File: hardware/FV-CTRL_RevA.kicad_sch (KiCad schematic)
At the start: 69 parts, among them J1 12V_IN, J10 IR_RX2, J11 IR_TX1 (Col 1), J12 IR_TX2 (Col 2), J13 LS1 (DNP), J14 LS2 (DNP), J15 LS3 (DNP), J16 LS4 (DNP), J17 I2C_RESERVED, J2 XL4015_A (6.0V >=5A), J3 XL4015_B (6.0V >=5A), J4 BUCK_5V (Logic), J5 S1_TOP, J6 S1_BOT, J7 S2_TOP, J8 S2_BOT, J9 IR_RX1, Q1 IRF9540N, Q2 S8050

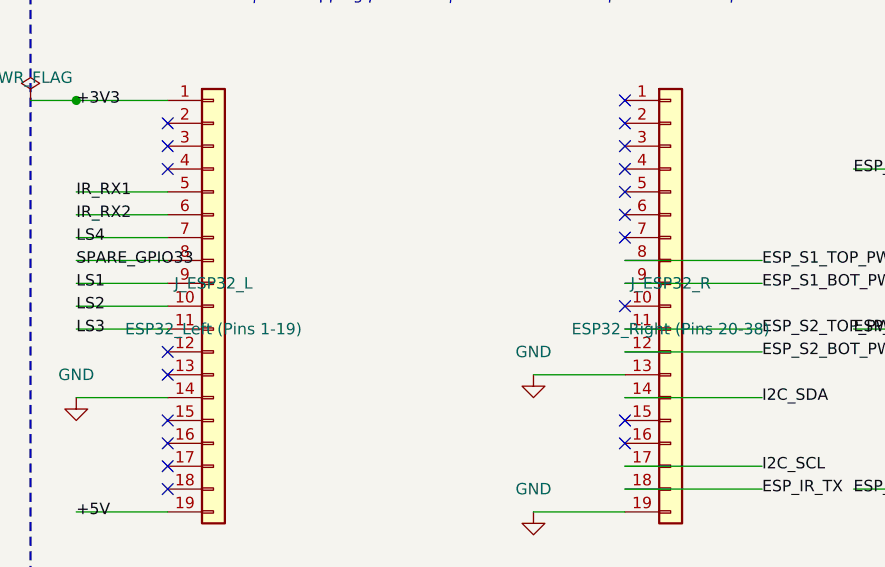
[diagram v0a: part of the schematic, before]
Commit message: fix(sch): standardize ESP32 header references to J18/J19 and update audit status
- Rename J_ESP32_L / J_ESP32_R to standard KiCad annotations J18 / J19
- Regenerate KiCad schematic, manifest, netlist JSON, draft BOM, and ERC reports
- Eliminate netlist export annotation warnings
- Update automated tests in test_code_generation.py for J18 and J19
- Resolve contradiction in audit_fv_project.py and audit-revA.md regarding schematic existence
- Track AGENTS.md rules
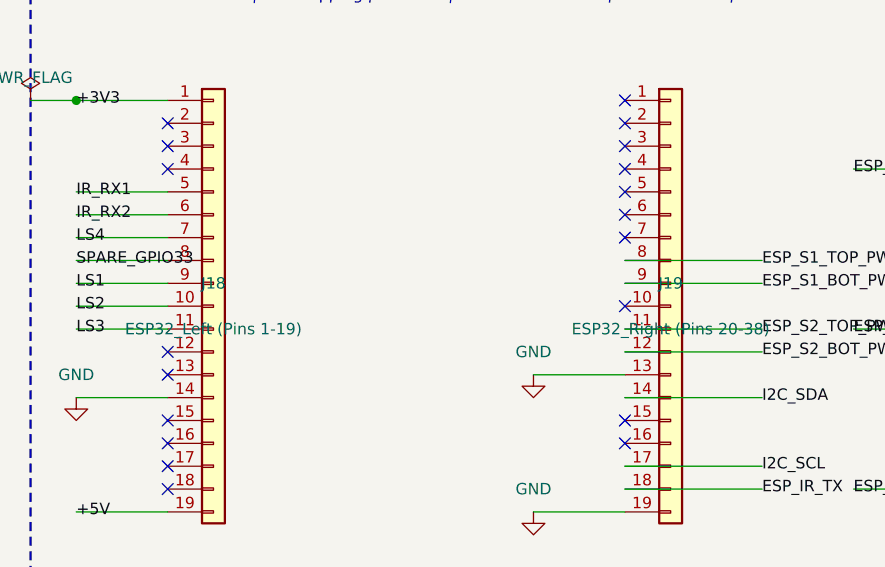
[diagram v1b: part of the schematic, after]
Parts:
- removed J_ESP32_L: ESP32_Left (Pins 1-19), symbol Connector_Generic:Conn_01x19
- removed J_ESP32_R: ESP32_Right (Pins 20-38), symbol Connector_Generic:Conn_01x19
- added J18: ESP32_Left (Pins 1-19), symbol Connector_Generic:Conn_01x19
- added J19: ESP32_Right (Pins 20-38), symbol Connector_Generic:Conn_01x19
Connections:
- net +3V3: now also J18.1 (Pin_1)
- net +5V: now also J18.19 (Pin_19)
- net ESP_IR_TX: now also J19.18 (Pin_18)
- net ESP_S1_BOT_PWM: now also J19.9 (Pin_9)
- net ESP_S1_TOP_PWM: now also J19.8 (Pin_8)
- net ESP_S2_BOT_PWM: now also J19.12 (Pin_12)
- net ESP_S2_TOP_PWM: now also J19.11 (Pin_11)
- net GND: now also J18.14 (Pin_14), J19.13 (Pin_13), J19.19 (Pin_19)
- net I2C_SCL: now also J19.17 (Pin_17)
- net I2C_SDA: now also J19.14 (Pin_14)
- net IR_RX1: now also J18.5 (Pin_5)
- net IR_RX2: now also J18.6 (Pin_6)
- net LS1: now also J18.9 (Pin_9)
- net LS2: now also J18.10 (Pin_10)
- net LS3: now also J18.11 (Pin_11)
- net LS4: now also J18.7 (Pin_7)
- net SPARE_GPIO33: now also J18.8 (Pin_8)
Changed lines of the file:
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@@
 		(on_board yes)
 		(dnp no)
-		(property "Reference" "J_ESP32_L"
+		(property "Reference" "J18"
 			(at 152.4000 154.9400 0)
 			(effects (font (size 1.27 1.27)))
@@
 		(on_board yes)
 		(dnp no)
-		(property "Reference" "J_ESP32_R"
+		(property "Reference" "J19"
 			(at 203.2000 154.9400 0)
 			(effects (font (size 1.27 1.27)))

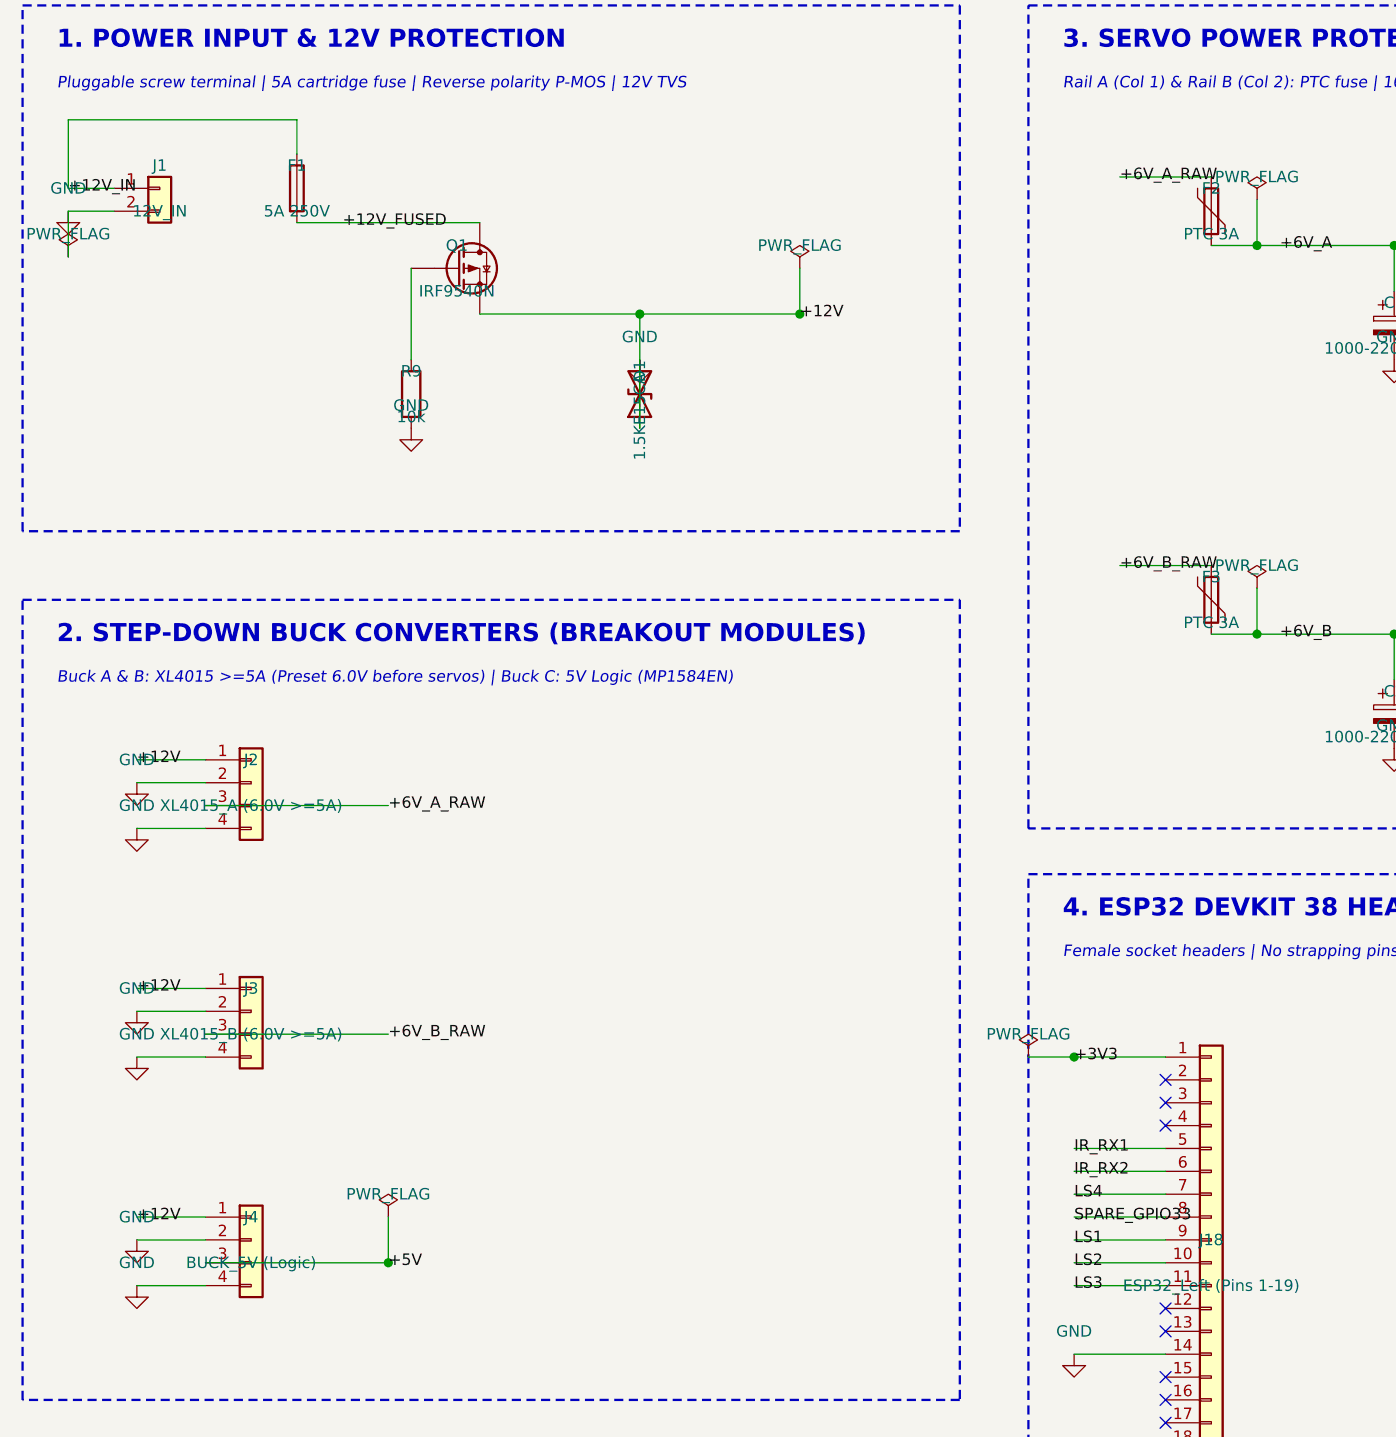
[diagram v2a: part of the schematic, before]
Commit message: feat(sch): synchronize schematics, manifests, and zero-violation ERC reports
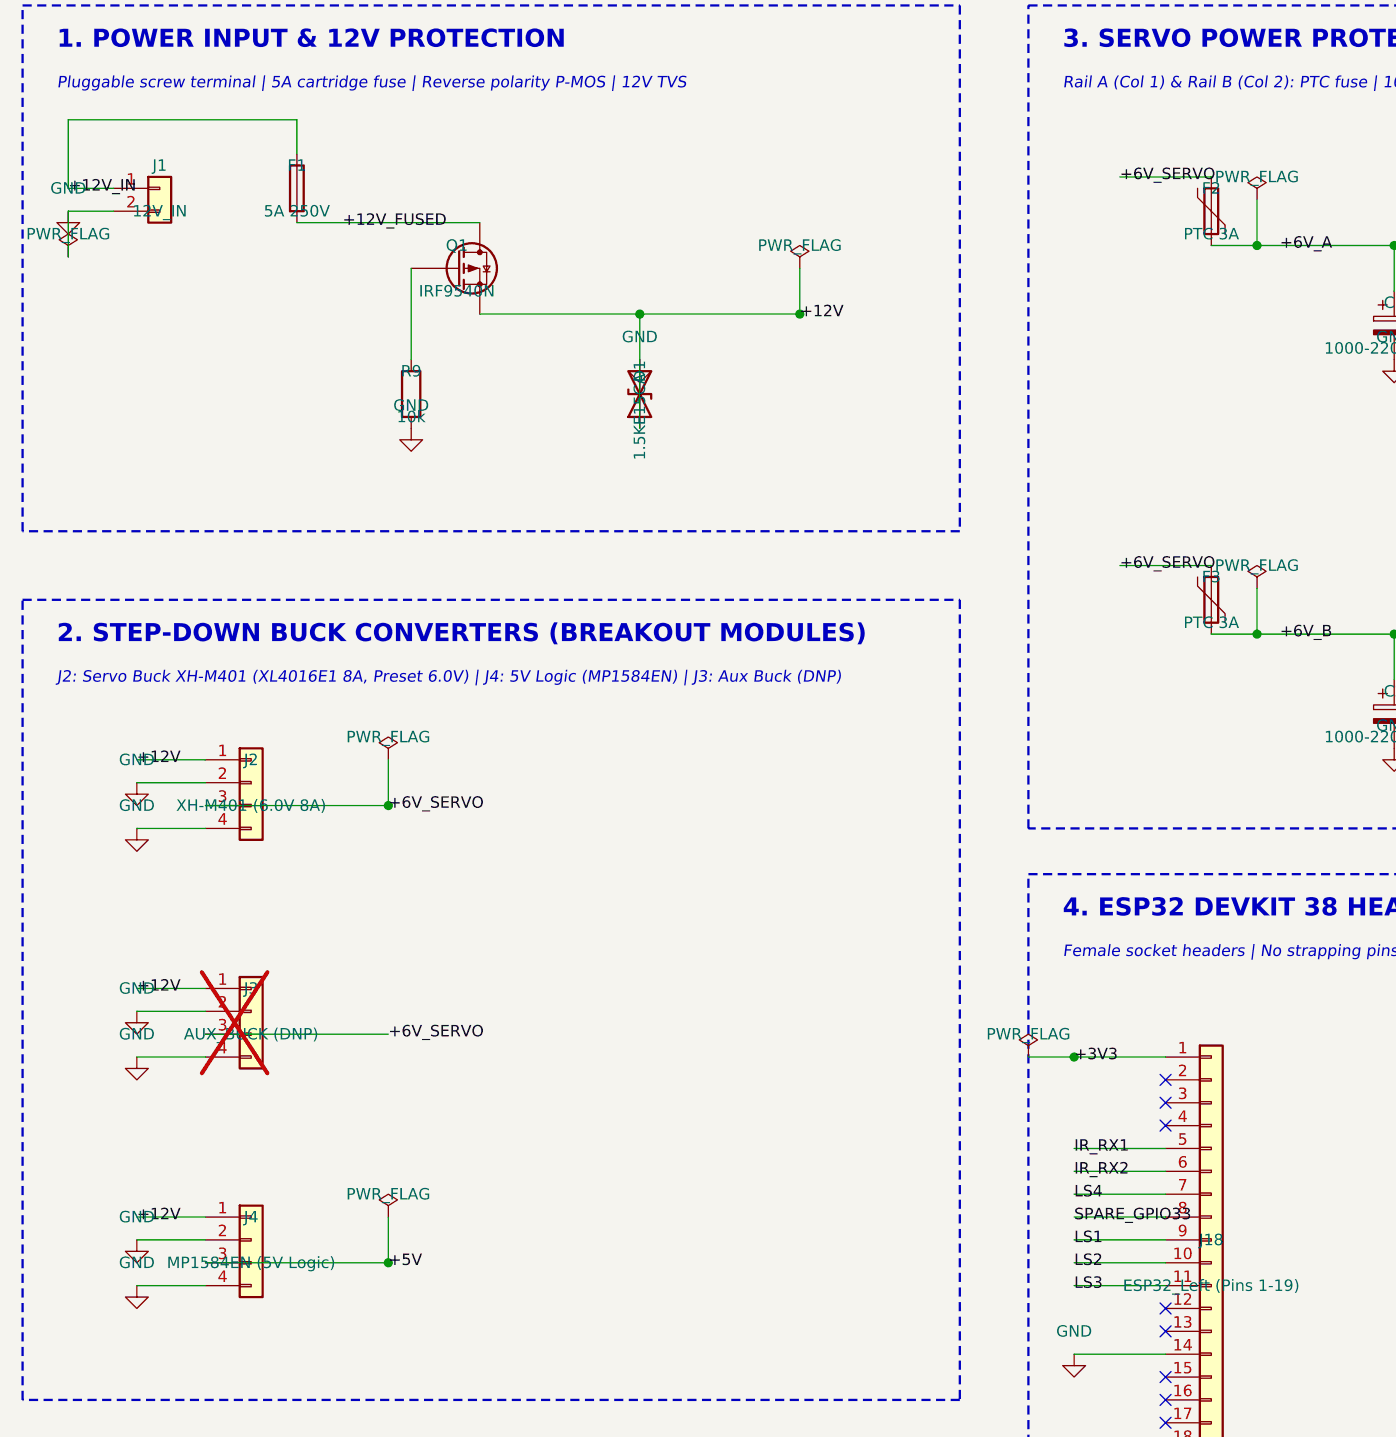
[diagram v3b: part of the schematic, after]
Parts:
- C1, C2: footprint (none) -> Capacitor_THT:CP_Radial_D12.5mm_P5.00mm
- C10, C3, C4, C5, C6, C7, C8, C9: footprint (none) -> Capacitor_THT:C_Disc_D5.0mm_W2.5mm_P5.00mm
- D1: footprint (none) -> Diode_THT:D_DO-201_P12.70mm_Horizontal
- D2, D3, D4, D5, D6: footprint (none) -> LED_THT:LED_D3.0mm
- F1: footprint (none) -> Fuse:Fuseholder_Clip-5x20mm_Littelfuse_111_Inline_P20.00x5.00mm_D1.05mm_Horizontal
- F2, F3: footprint (none) -> Fuse:Fuse_Bourns_MF-RG300
- J1: footprint (none) -> TerminalBlock_Phoenix:TerminalBlock_Phoenix_MKDS-1,5-2-5.08_1x02_P5.08mm_Horizontal
- J10, J9: footprint (none) -> Connector_JST:JST_XH_B3B-XH-A_1x03_P2.50mm_Vertical
- J11, J12, J13, J14, J15, J16: footprint (none) -> Connector_JST:JST_XH_B2B-XH-A_1x02_P2.50mm_Vertical
- J17: footprint (none) -> Connector_PinHeader_2.54mm:PinHeader_1x04_P2.54mm_Vertical
- J18, J19: footprint (none) -> Connector_PinSocket_2.54mm:PinSocket_1x19_P2.54mm_Vertical
- J2: value XL4015_A (6.0V >=5A) -> XH-M401 (6.0V 8A); footprint (none) -> fv_modules:Converter_DCDC_XH-M401_8A
- J3: value XL4015_B (6.0V >=5A) -> AUX_BUCK (DNP); footprint (none) -> Connector_PinHeader_2.54mm:PinHeader_1x04_P2.54mm_Vertical; now not fitted
- J4: value BUCK_5V (Logic) -> MP1584EN (5V Logic); footprint (none) -> fv_modules:Converter_DCDC_MP1584EN
- J5, J6, J7, J8: footprint (none) -> Connector_PinHeader_2.54mm:PinHeader_1x03_P2.54mm_Vertical
- Q1: footprint (none) -> Package_TO_SOT_THT:TO-220-3_Vertical
- Q2: footprint (none) -> Package_TO_SOT_THT:TO-92_Inline
- R1, R13, R14, R15, R16, R17, R18, R19, R2, R20, R21, R22, R23, R24, R3, R4, R5, R6, R7, R8, R9: footprint (none) -> Resistor_THT:R_Axial_DIN0207_L6.3mm_D2.5mm_P7.62mm_Horizontal
- TP1, TP2, TP3, TP4, TP5, TP6, TP7, TP8: footprint (none) -> TestPoint:TestPoint_Pad_D2.0mm
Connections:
- net +6V_B_RAW is gone; now on net +6V_SERVO: F3.1, J3.3 (Pin_3)
- net +6V_A_RAW renamed +6V_SERVO
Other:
- note added: "J2: Servo Buck XH-M401 (XL4016E1 8A, Preset 6.0V) | J4: 5V Logic (MP1584EN) | J3: Aux Buck (DNP)"
- note removed: "Buck A & B: XL4015 >=5A (Preset 6.0V before servos) | Buck C: 5V Logic (MP1584EN)"
